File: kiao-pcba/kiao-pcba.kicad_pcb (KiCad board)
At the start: 2 copper layers, 17.8 x 21 mm, 20 parts, among them J1 USB_C_Receptacle_USB2.0, SW1 BOOT, U1 STM32F072CBT6, U3 xiao_drop-in_gpio_usb_no_cuto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, U4 XC6206PxxxMR-Regulator_Linear, U5 PRTR5V0U2X

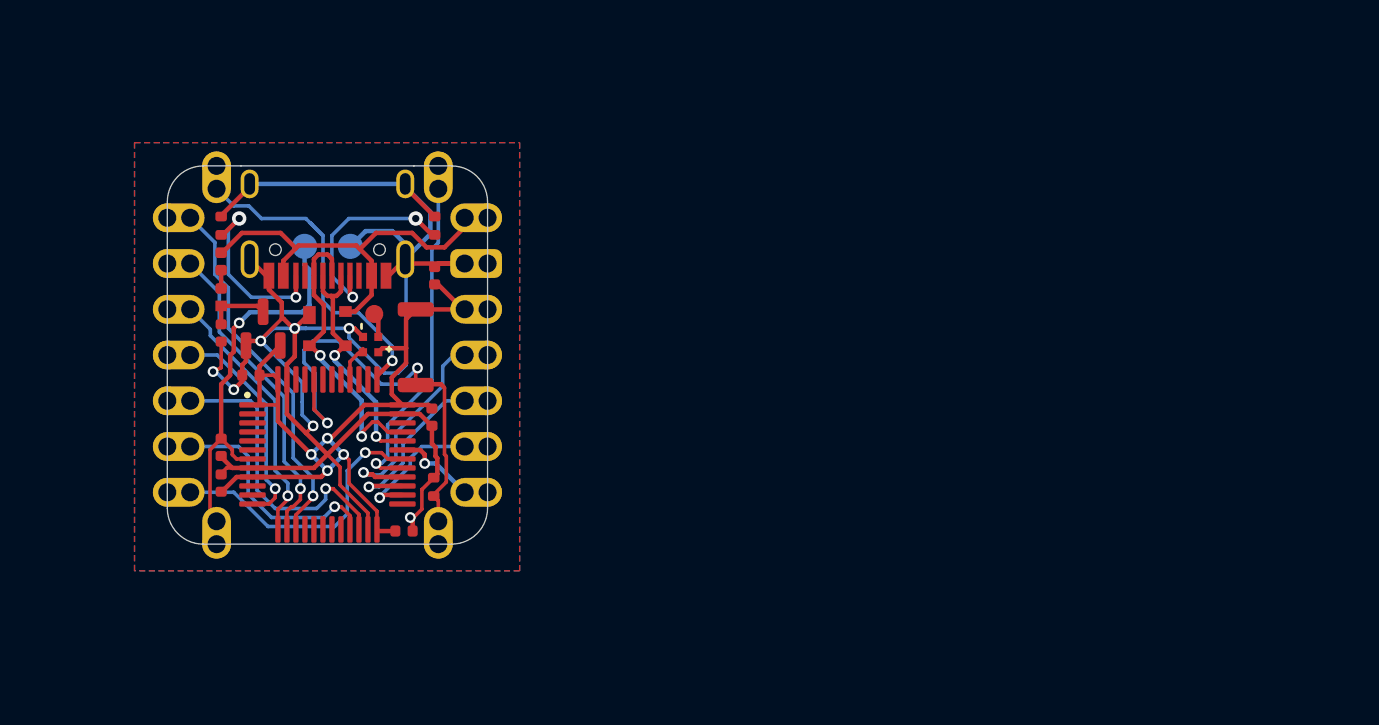
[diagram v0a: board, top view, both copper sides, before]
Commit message: Changes pinout, half-panel, gerbers. Proto'd
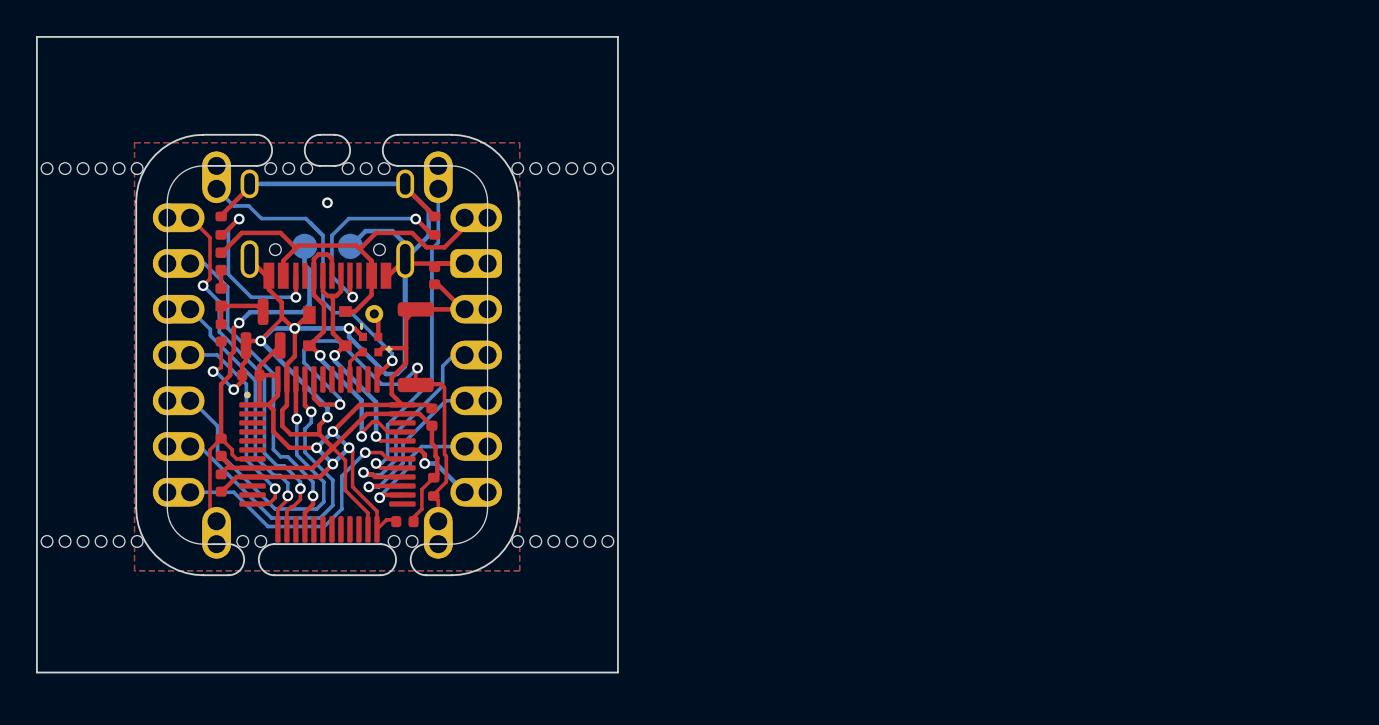
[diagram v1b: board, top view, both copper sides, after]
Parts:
- added ?: , , F.Cu at (87.4, 103.6)
- added ?: , , F.Cu at (85.4, 103.6)
- added ?: , , F.Cu at (86.4, 82.9)
- added ?: , , F.Cu at (85.4, 82.9)
- added ?: , , F.Cu at (113.6, 103.6)
- added ?: , , F.Cu at (88.4, 103.6)
- added ?: , , F.Cu at (101.1, 82.9)
- added ?: , , F.Cu at (110.6, 82.9)
- added ?: , , F.Cu at (89.4, 103.6)
- added ?: , , F.Cu at (84.4, 103.6)
- added ?: , , F.Cu at (102.1, 82.9)
- added ?: , , F.Cu at (98.9, 82.9)
- added ?: , , F.Cu at (111.6, 82.9)
- added ?: , , F.Cu at (111.6, 103.6)
- added ?: , , F.Cu at (97.9, 82.9)
- added ?: , , F.Cu at (86.4, 103.6)
- added ?: , , F.Cu at (88.4, 82.9)
- added ?: , , F.Cu at (87.4, 82.9)
- added ?: , , F.Cu at (89.4, 82.9)
- added ?: , , F.Cu at (112.6, 103.6)
- added ?: , , F.Cu at (103.1, 82.9)
- added ?: , , F.Cu at (95.3, 103.6)
- added ?: , , F.Cu at (112.6, 82.9)
- added ?: , , F.Cu at (96.3, 103.6)
- added ?: , , F.Cu at (115.6, 103.6)
- added ?: , , F.Cu at (96.9, 82.9)
- added ?: , , F.Cu at (113.6, 82.9)
- added ?: , , F.Cu at (103.7, 103.6)
- added ?: , , F.Cu at (114.6, 103.6)
- added ?: , , F.Cu at (84.4, 82.9)
- added ?: , , F.Cu at (110.6, 103.6)
- added ?: , , F.Cu at (114.6, 82.9)
- added ?: , , F.Cu at (104.7, 103.6)
- added ?: , , F.Cu at (115.6, 82.9)
- TP1: footprint TestPoint:TestPoint_Pad_D1.0mm -> TestPoint:TestPoint_THTPad_D1.0mm_Drill0.5mm
- moved C6 0.52 mm to (104.3, 102.5)
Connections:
- U3 pad 1: /A5 -> /A4
- U3 pad 2: /A4 -> /A6
- U3 pad 5: /B11 -> /B9
- U3 pad 6: /B10 -> /B8
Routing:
- net /A5: track 20.5 -> 0.00 mm, vias 1 -> 0
- net /A6: track 0.00 -> 18.4 mm, vias 0 -> 1
- net /B9: track 0.00 -> 18.2 mm, vias 0 -> 1
- net /B8: track 0.00 -> 17.2 mm, vias 0 -> 1
- net /B11: track 16.8 -> 0.00 mm, vias 1 -> 0
- net /B10: track 13.0 -> 0.00 mm, vias 1 -> 0
- net GND: track 101.6 -> 113.6 mm
- net /A4: track 17.7 -> 20.8 mm, vias 1 -> 2
- net +3V3: track 47.6 -> 48.6 mm
- net BOOT: track 25.6 -> 24.8 mm
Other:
- board size 17.8 x 21 mm -> 32.3 x 35.3 mm

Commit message: separated panelization
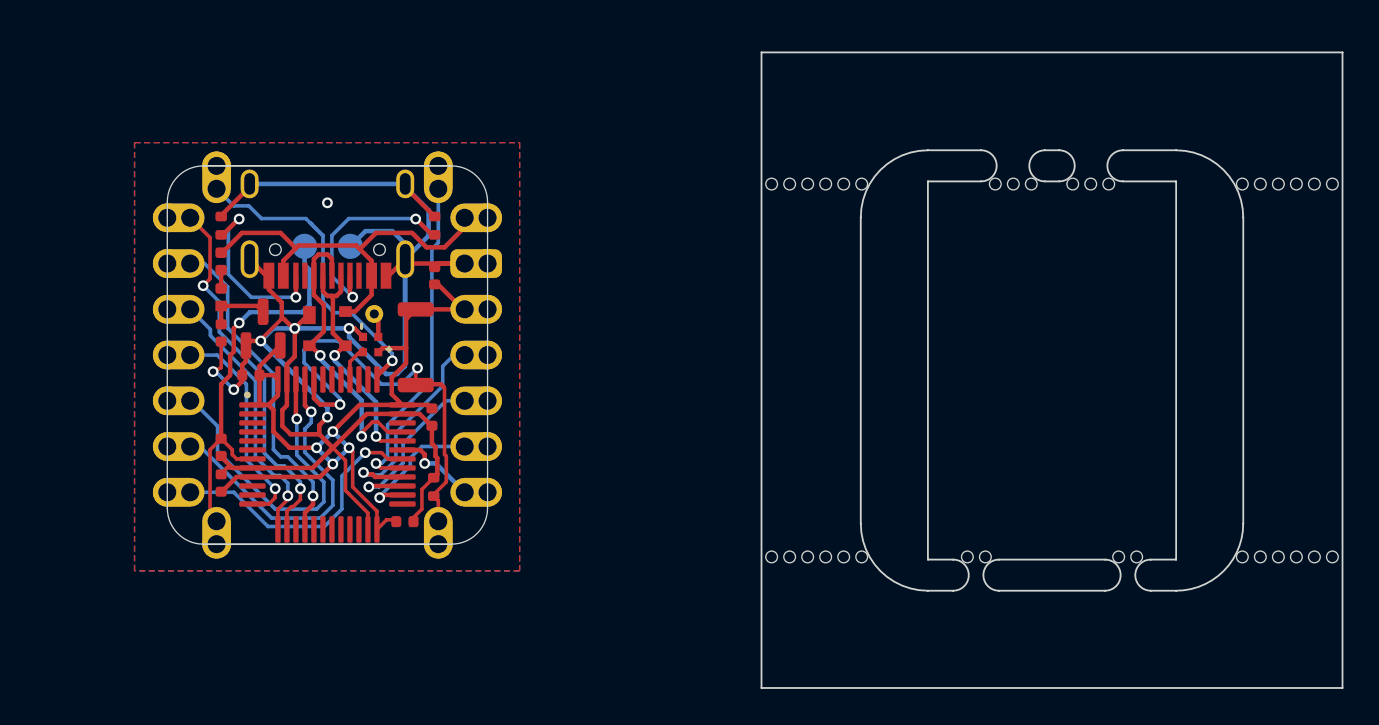
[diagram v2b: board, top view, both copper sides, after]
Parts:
- moved ? 40.2 mm to (127.7, 104.5)
- moved ? 40.2 mm to (125.7, 104.5)
- moved ? 40.2 mm to (126.7, 83.8)
- moved ? 40.2 mm to (125.7, 83.8)
- moved ? 40.2 mm to (153.8, 104.5)
- moved ? 40.2 mm to (128.7, 104.5)
- moved ? 40.2 mm to (141.4, 83.8)
- moved ? 40.2 mm to (150.8, 83.8)
- moved ? 40.2 mm to (129.7, 104.5)
- moved ? 40.2 mm to (124.7, 104.5)
- moved ? 40.2 mm to (142.4, 83.8)
- moved ? 40.2 mm to (139.1, 83.8)
- moved ? 40.2 mm to (151.8, 83.8)
- moved ? 40.2 mm to (151.8, 104.5)
- moved ? 40.2 mm to (138.1, 83.8)
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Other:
- board size 32.3 x 35.3 mm -> 63.2 x 35.3 mm
